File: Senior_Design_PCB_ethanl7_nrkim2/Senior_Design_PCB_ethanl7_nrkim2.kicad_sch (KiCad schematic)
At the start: 15 parts, among them U1 uA7805, U2 LM386, U3 L298N, U4 L298N, U5 L298N, U6 STM32H7B0RBTx, U7 LM2937xT

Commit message: changes to schematic
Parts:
- C1: value C -> .33 uF
- C2, C3: value C -> .1 uF
- C4: value C -> 10 uF
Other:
- moved on the sheet: C1
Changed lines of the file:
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@@
 	)
 	(junction
-		(at 53.34 50.8)
+		(at 49.53 50.8)
 		(diameter 0)
 		(color 0 0 0 0)
@@
 	(wire
 		(pts
-			(xy 53.34 62.23) (xy 64.77 62.23)
+			(xy 49.53 62.23) (xy 64.77 62.23)
 		)
 		(stroke
@@
 	(wire
 		(pts
-			(xy 53.34 50.8) (xy 57.15 50.8)
-		)
-		(stroke
-			(width 0)
-			(type default)
-		)
-	)
-	(wire
-		(pts
 			(xy 160.02 254) (xy 160.02 259.08)
 		)
@@
 	(wire
 		(pts
+			(xy 49.53 50.8) (xy 57.15 50.8)
+		)
+		(stroke
+			(width 0)
+			(type default)
+		)
+	)
+	(wire
+		(pts
 			(xy 80.01 213.36) (xy 80.01 218.44)
 		)
@@
 	(wire
 		(pts
-			(xy 53.34 52.07) (xy 53.34 50.8)
-		)
-		(stroke
-			(width 0)
-			(type default)
-		)
-	)
-	(wire
-		(pts
-			(xy 45.72 50.8) (xy 53.34 50.8)
+			(xy 49.53 52.07) (xy 49.53 50.8)
+		)
+		(stroke
+			(width 0)
+			(type default)
+		)
+	)
+	(wire
+		(pts
+			(xy 45.72 50.8) (xy 49.53 50.8)
 		)
 		(stroke
@@
 	(wire
 		(pts
-			(xy 53.34 62.23) (xy 53.34 59.69)
+			(xy 49.53 62.23) (xy 49.53 59.69)
 		)
 		(stroke
@@
 			)
 		)
-		(property "Value" "C"
+		(property "Value" ".1 uF"
 			(at 81.28 57.1499 0)
 			(effects
@@
 			)
 		)
-		(property "Value" "C"
+		(property "Value" ".1 uF"
 			(at 114.3 58.4199 0)
 			(effects
@@
 	(symbol
 		(lib_id "Device:C")
-		(at 53.34 55.88 0)
+		(at 49.53 55.88 0)
 		(unit 1)
 		(exclude_from_sim no)
@@
 		(fields_autoplaced yes)
 		(property "Reference" "C1"
-			(at 57.15 54.6099 0)
+			(at 53.34 54.6099 0)
 			(effects
 				(font
@@
 			)
 		)
-		(property "Value" "C"
-			(at 57.15 57.1499 0)
+		(property "Value" ".33 uF"
+			(at 53.34 57.1499 0)
 			(effects
 				(font
@@
 		)
 		(property "Footprint" ""
-			(at 54.3052 59.69 0)
+			(at 50.4952 59.69 0)
 			(effects
 				(font
@@
 		)
 		(property "Datasheet" "~"
-			(at 53.34 55.88 0)
+			(at 49.53 55.88 0)
 			(effects
 				(font
@@
 		)
 		(property "Description" "Unpolarized capacitor"
-			(at 53.34 55.88 0)
+			(at 49.53 55.88 0)
 			(effects
 				(font
@@
 			)
 		)
-		(property "Value" "C"
+		(property "Value" "10 uF"
 			(at 138.43 58.4199 0)
 			(effects

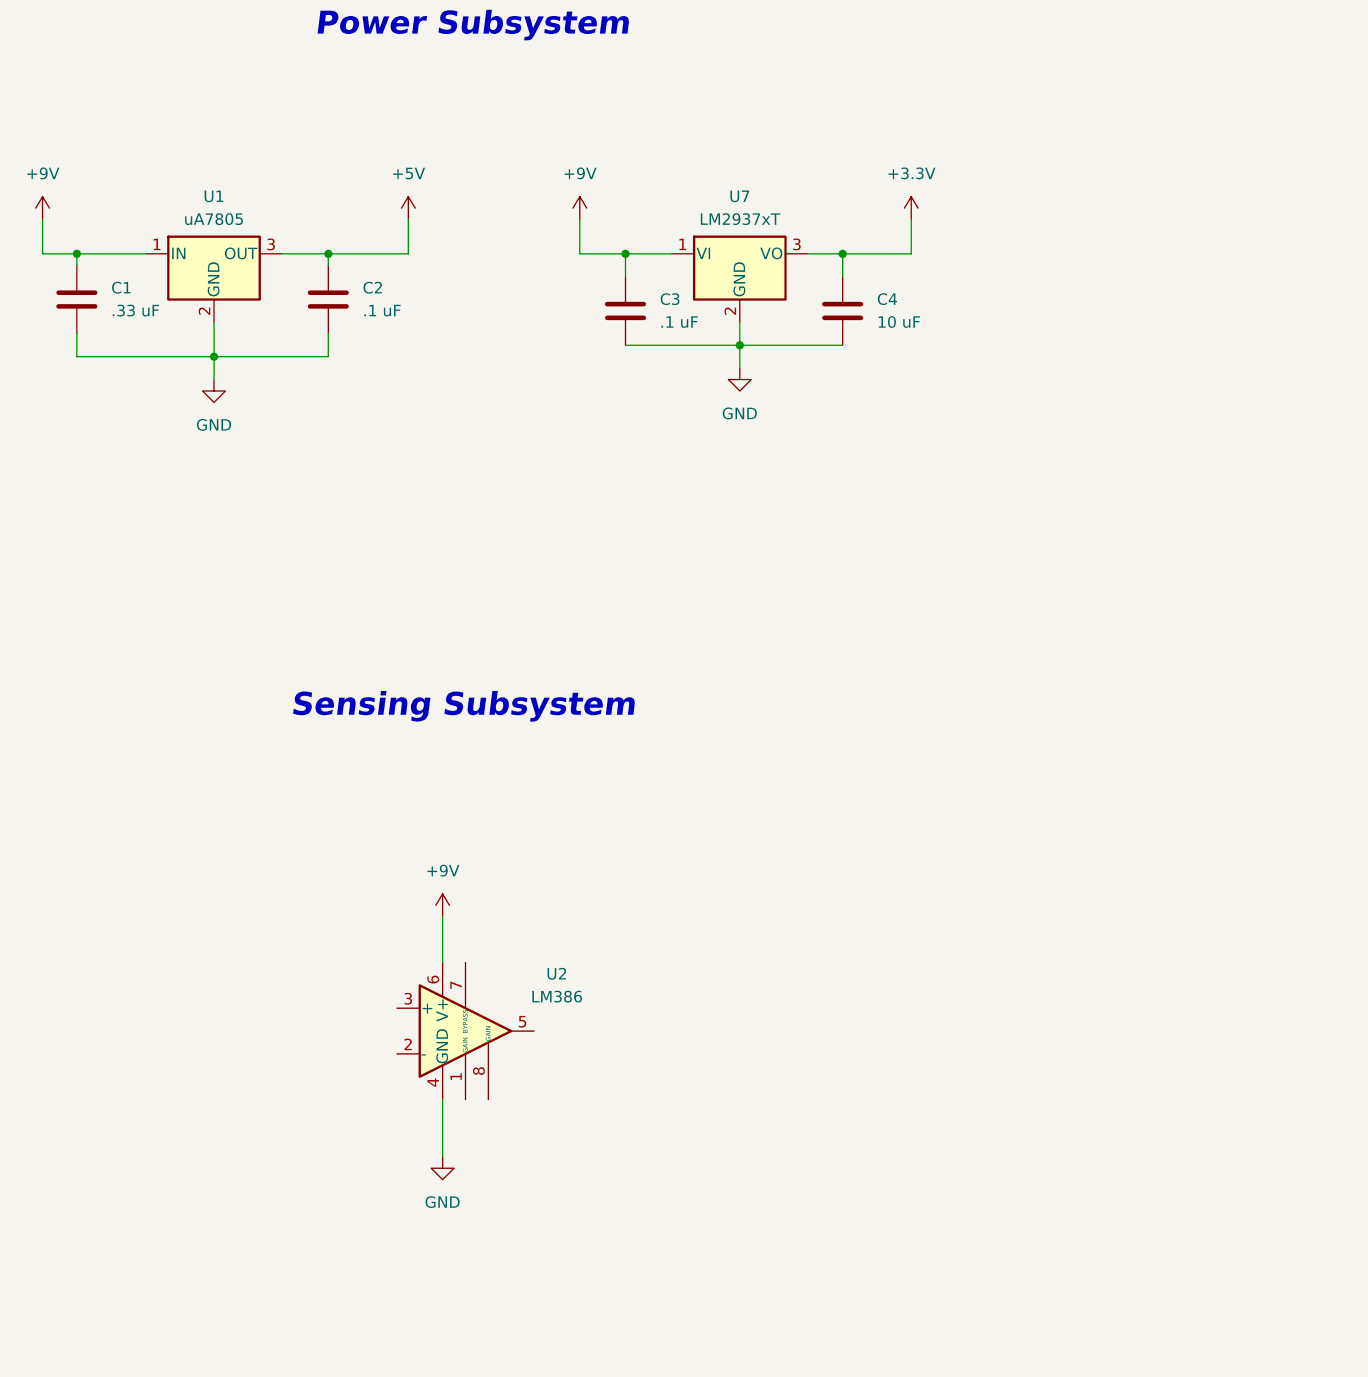
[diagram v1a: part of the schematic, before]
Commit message: schematic power supply and sensing
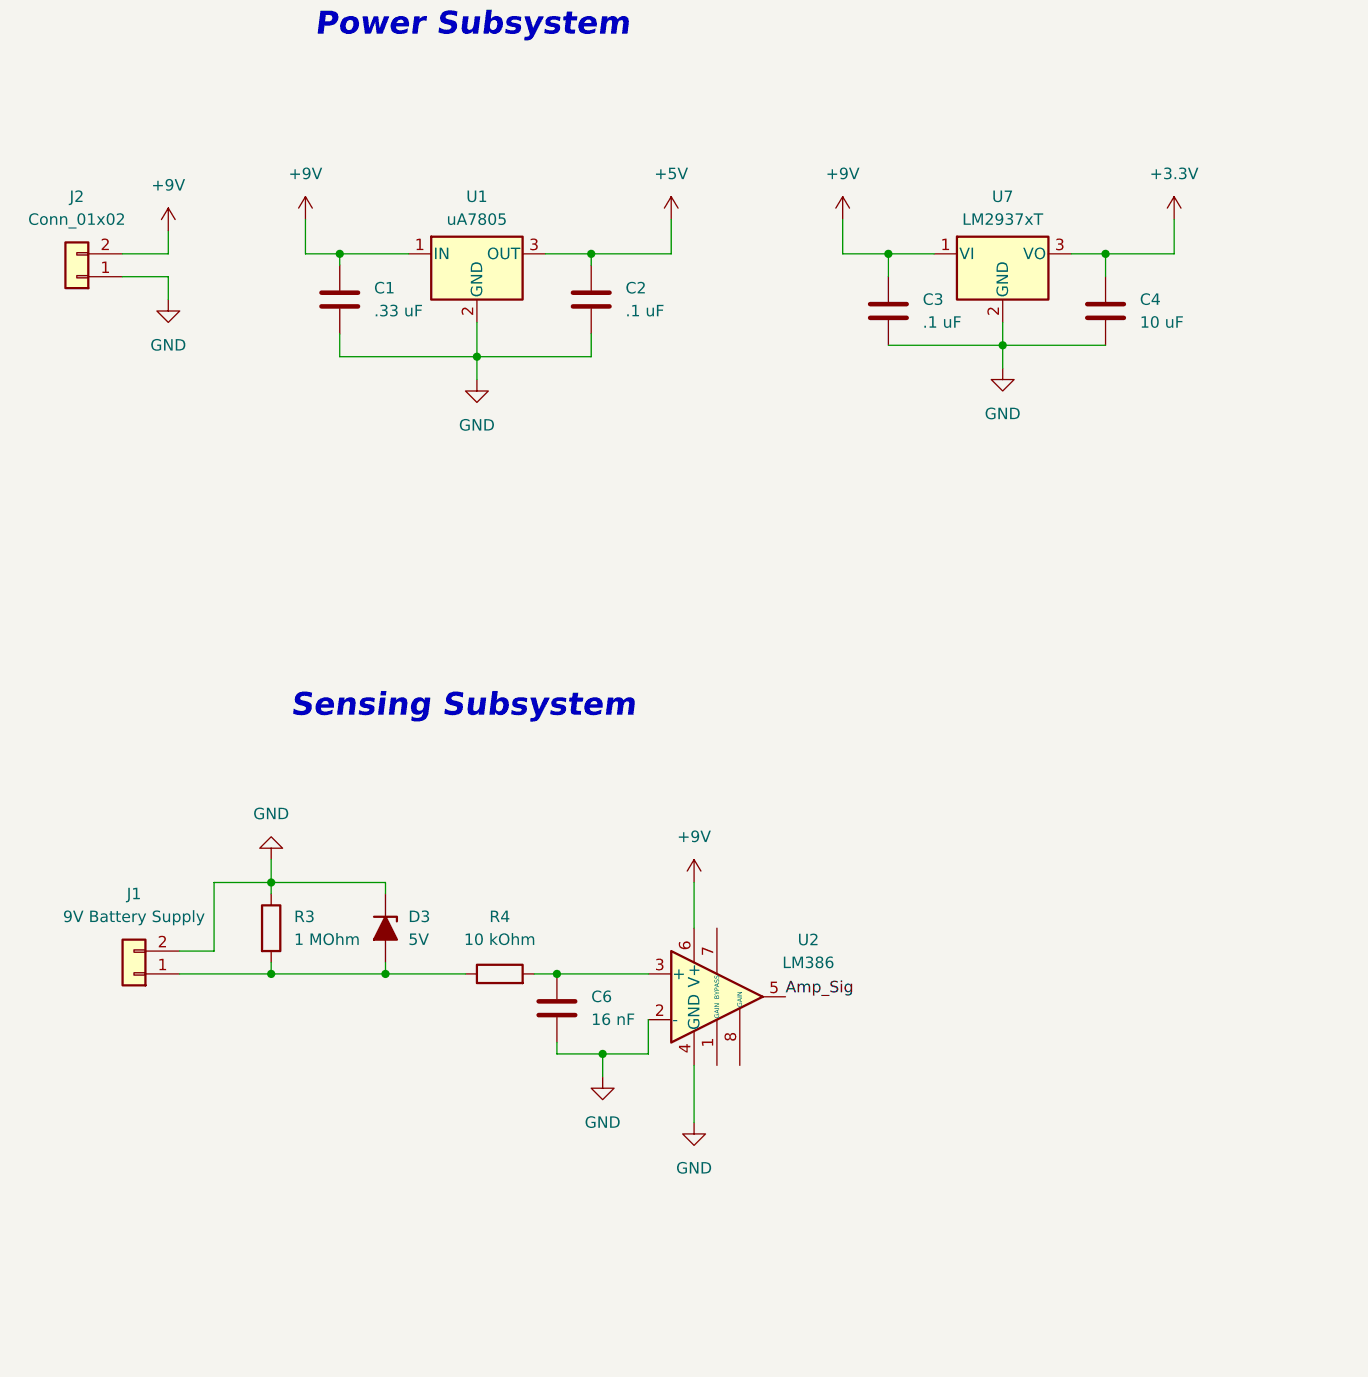
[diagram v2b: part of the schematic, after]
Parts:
- added C6: 16 nF, symbol Device:C
- added D3: 5V, symbol Device:D_Zener_Filled
- added J1: 9V Battery Supply, symbol Connector_Generic:Conn_01x02
- added J2: Conn_01x02, symbol Connector_Generic:Conn_01x02
- added R3: 1 MOhm, symbol Device:R
- added R4: 10 kOhm, symbol Device:R
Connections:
- net +9V: now also J2.2 (Pin_2)
- net GND: now also U2.2 (-), C6.1, D3.1 (K), J1.2 (Pin_2), J2.1 (Pin_1), R3.1
- net at U2.3 (+): now also C6.2, R4.2
- net Amp_Sig: now reaches U2.5
- new net: D3.2 (A), J1.1 (Pin_1), R3.2, R4.1
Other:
- moved on the sheet: C1, C2, C3, C4, U1, U2, U7

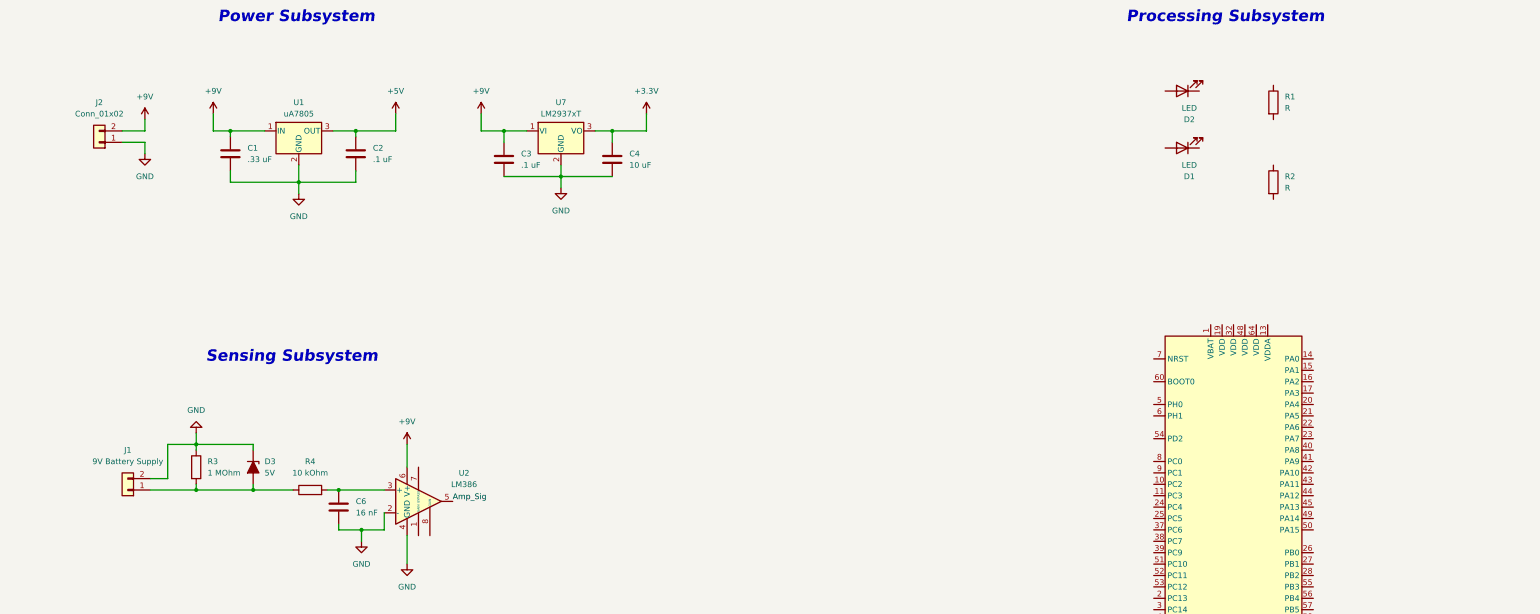
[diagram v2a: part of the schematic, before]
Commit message: scopy spectrogram data, slight updates to magnet mount and PCB schematic
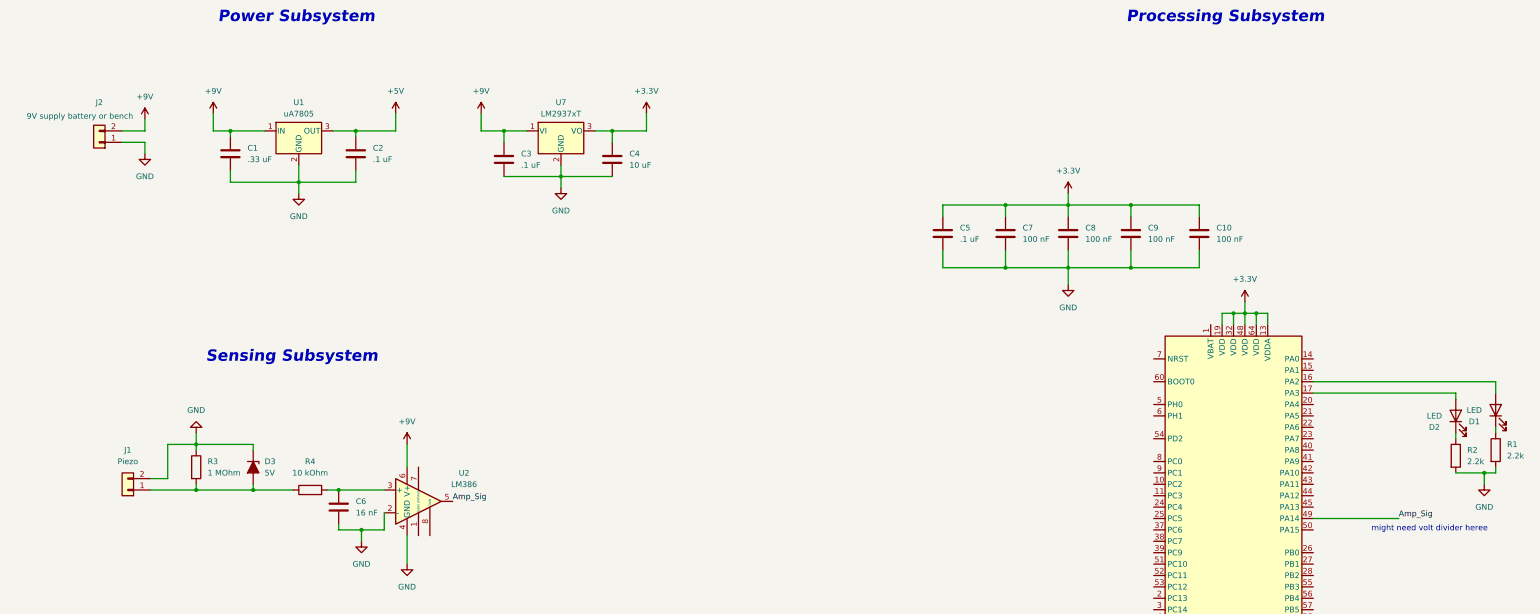
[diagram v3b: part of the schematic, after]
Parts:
- added C10, C7, C8, C9: 100 nF, symbol Device:C
- added C5: .1 uF, symbol Device:C
- J1: value 9V Battery Supply -> Piezo
- J2: value Conn_01x02 -> 9V supply battery or bench
- R1, R2: value R -> 2.2k
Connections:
- net +3.3V: now also U6.13 (VDDA), U6.19 (VDD), U6.32 (VDD), U6.48 (VDD), U6.64 (VDD), C10.1, C5.1, C7.1, C8.1, C9.1
- net Amp_Sig: now also U6.49 (PA14)
- net GND: now also R1.2, R2.2, C10.2, C5.2, C7.2, C8.2, C9.2
- net at D1.1 (K): now also R1.1
- net at D1.2 (A): now also U6.16 (PA2)
- net at U6.17 (PA3): now also D2.2 (A)
- net at D2.1 (K): now also R2.1
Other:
- note added: "might need volt divider heree"
- moved on the sheet: D1, D2, R1, R2

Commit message: schematic updates
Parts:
- added C11, C12: 1 uF, symbol Device:C
- added D4: MBR0520, Diode_SMD:D_SOD-123, symbol Diode:MBR0520
- added J3: Conn_02x03_Odd_Even, symbol Connector_Generic:Conn_02x03_Odd_Even
- added J4: Conn_ARM_JTAG_SWD_10, symbol Connector:Conn_ARM_JTAG_SWD_10
- added R10, R8, R9: 100 kOhm, symbol Device:R
- added R5, R6, R7: 10 kOhm, symbol Device:R
- added SW1: SW_Push, symbol Switch:SW_Push
- added TP1: GND, symbol Connector:TestPoint
- C10: value 100 nF -> 10 nF
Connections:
- net +3.3V: now also U6.60 (BOOT0), C11.1, J3.1 (Pin_1), J3.2 (Pin_2), R5.1
- net Amp_Sig: now also U6.8 (PC0); no longer U6.49 (PA14)
- net GND: now also U6.12 (VSSA), U6.18 (VSS), U6.31 (VSS), U6.47 (VSS), U6.63 (VSS), C11.2, C12.2, J3.5 (Pin_5), J3.6 (Pin_6), J4.3 (GND), J4.5 (GND), J4.9 (GNDDetect), R6.1, R7.2, SW1.1, TP1.1
- net JTMS/SWDIO: now reaches U6.45 (PA13)
- net JTMS/SWDIO: now also J4.2 (SWDIO/TMS), R9.1
- net JTDI: now reaches U6.50 (PA15)
- net JTDI: now also J4.8 (NC/TDI)
- net JTDO/TRACESWO: now reaches U6.55 (PB3)
- net JTDO/TRACESWO: now also J4.6 (SWO/TDO), R10.1
- net NRST: now reaches U6.7 (NRST)
- net NRST: now also C12.1, J4.10 (~{RESET}), R5.2, SW1.2
- new net: J3.3 (Pin_3), R6.2
- new net: D4.1 (K), R10.2, R8.2, R9.2
- new net: J3.4 (Pin_4), R7.1
- new net: D4.2 (A), J4.1 (VTref)
- new net JTCK/SWCLK: J4.4 (SWCLK/TCK), R8.1, U6.49 (PA14)
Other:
- note added: "might need volt divider"
- note removed: "might need volt divider heree"
- moved on the sheet: C5, C7, C8, C9, D1, D2, R1, R2, U3, U4, U5, U6

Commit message: finished schematic, started pcb
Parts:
- added C13, C14, C15, C16, C17, C18: 100 nF, Capacitor_SMD:C_0805_2012Metric_Pad1.18x1.45mm_HandSolder, symbol Device:C
- added D10, D11, D12, D13, D14, D15, D16, D17, D18, D19, D20, D21, D22, D23, D24, D25, D26, D27, D28, D5, D6, D7, D8, D9: 1N5817, Diode_THT:D_DO-41_SOD81_P10.16mm_Horizontal, symbol Diode:1N5817
- added H1, H2, H3, H4: MountingHole, MountingHole:MountingHole_3.2mm_M3, symbol Mechanical:MountingHole
- added J10: M6, Connector_Molex:Molex_KK-254_AE-6410-02A_1x02_P2.54mm_Vertical, symbol Connector_Generic:Conn_01x02
- added J5: M1, Connector_Molex:Molex_KK-254_AE-6410-02A_1x02_P2.54mm_Vertical, symbol Connector_Generic:Conn_01x02
- added J6: M2, Connector_Molex:Molex_KK-254_AE-6410-02A_1x02_P2.54mm_Vertical, symbol Connector_Generic:Conn_01x02
- added J7: M3, Connector_Molex:Molex_KK-254_AE-6410-02A_1x02_P2.54mm_Vertical, symbol Connector_Generic:Conn_01x02
- added J8: M4, Connector_Molex:Molex_KK-254_AE-6410-02A_1x02_P2.54mm_Vertical, symbol Connector_Generic:Conn_01x02
- added J9: M5, Connector_Molex:Molex_KK-254_AE-6410-02A_1x02_P2.54mm_Vertical, symbol Connector_Generic:Conn_01x02
- added TP2: AMP, TestPoint:TestPoint_Pad_D1.5mm, symbol Connector:TestPoint
- added TP3: LPF, TestPoint:TestPoint_Pad_D1.5mm, symbol Connector:TestPoint
- added TP4: Reg_5, TestPoint:TestPoint_Pad_D1.5mm, symbol Connector:TestPoint
- added TP5: Reg_3, TestPoint:TestPoint_Pad_D1.5mm, symbol Connector:TestPoint
- C1, C10, C11, C12, C2, C3, C4, C5, C6, C7, C8, C9: footprint (none) -> Capacitor_SMD:C_0805_2012Metric_Pad1.18x1.45mm_HandSolder
- D1, D2: footprint (none) -> LED_SMD:LED_0805_2012Metric_Pad1.15x1.40mm_HandSolder
- D3: value 5V -> 5V_Znr; footprint (none) -> Diode_THT:D_DO-41_SOD81_P10.16mm_Horizontal
- J1, J2: footprint (none) -> Connector_Molex:Molex_KK-254_AE-6410-02A_1x02_P2.54mm_Vertical
- J3: footprint (none) -> Connector_PinSocket_2.54mm:PinSocket_2x03_P2.54mm_Vertical
- J4: footprint (none) -> Connector_IDC:IDC-Header_2x05_P2.54mm_Vertical
- R1, R10, R2, R3, R4, R5, R6, R7, R8, R9: footprint (none) -> Resistor_SMD:R_0805_2012Metric_Pad1.20x1.40mm_HandSolder
- SW1: footprint (none) -> Button_Switch_SMD:SW_SPST_B3S-1000
- TP1: footprint (none) -> TestPoint:TestPoint_Pad_D1.5mm
- U1: footprint (none) -> Package_TO_SOT_THT:TO-220-3_Vertical
- U2: footprint (none) -> Package_DIP:DIP-8_W7.62mm
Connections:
- net +3.3V: now also D4.1 (K), R10.2, R8.2, R9.2, TP5.1
- net +5V: now also U2.6 (V+), U3.9 (Vss), U4.9 (Vss), U5.9 (Vss), C13.2, C15.2, C17.2, D11.1 (K), D13.1 (K), D15.1 (K), D17.1 (K), D19.1 (K), D21.1 (K), D23.1 (K), D25.1 (K), D27.1 (K), D7.1 (K), D8.1 (K), D9.1 (K), TP4.1; no longer U3.4 (Vs), U4.4 (Vs), U5.4 (Vs)
- net +9V: now also U3.4 (Vs), U4.4 (Vs), U5.4 (Vs), C14.1, C16.1, C18.1; no longer U2.6 (V+)
- net Amp_Sig: now also TP2.1
- net GND: now also C13.1, C14.2, C15.1, C16.2, C17.1, C18.2, D10.2 (A), D12.2 (A), D14.2 (A), D16.2 (A), D18.2 (A), D20.2 (A), D22.2 (A), D24.2 (A), D26.2 (A), D28.2 (A), D5.2 (A), D6.2 (A)
- net at D1.2 (A): now also U6.57 (PB5); no longer U6.16 (PA2)
- net M4P: now reaches U4.10 (IN3)
- net M4P: now also U6.37 (PC6)
- net M4En: now reaches U4.11 (EnB)
- net M4En: now also U6.17 (PA3)
- net M4N: now reaches U4.12 (IN4)
- net M4N: now also U6.38 (PC7)
- net at U4.13 (OUT3): now also D17.2 (A), D18.1 (K), J8.1 (Pin_1)
- net at U4.14 (OUT4): now also D19.2 (A), D20.1 (K), J8.2 (Pin_2)
- net at U4.2 (OUT1): now also D13.2 (A), D14.1 (K), J7.1 (Pin_1)
- net at U4.3 (OUT2): now also D15.2 (A), D16.1 (K), J7.2 (Pin_2)
- net M3P: now reaches U4.5 (IN1)
- net M3P: now also U6.35 (PB14)
- net M3En: now reaches U4.6 (EnA)
- net M3En: now also U6.16 (PA2)
- net M3N: now reaches U4.7 (IN2)
- net M3N: now also U6.36 (PB15)
- net at C6.2, R4.2, U2.3 (+): now also TP3.1
- net M1En: now reaches U6.14 (PA0)
- net M1En: now also U3.6 (EnA)
- net M2En: now reaches U6.15 (PA1)
- net M2En: now also U3.11 (EnB)
- net at D2.2 (A): now also U6.58 (PB6); no longer U6.17 (PA3)
- net M5En: now reaches U6.23 (PA7)
- net M5En: now also U5.6 (EnA)
- net M6En: now reaches U6.26 (PB0)
- net M6En: now also U5.11 (EnB)
- net M1P: now reaches U6.27 (PB1)
- net M1P: now also U3.5 (IN1)
- net M1N: now reaches U6.28 (PB2)
- net M1N: now also U3.7 (IN2)
- net M2P: now reaches U6.29 (PB10)
- net M2P: now also U3.10 (IN3)
- net M2N: now reaches U6.33 (PB12)
- net M2N: now also U3.12 (IN4)
- net M5P: now reaches U6.41 (PA9)
- net M5P: now also U5.5 (IN1)
- net M5N: now reaches U6.42 (PA10)
- net M5N: now also U5.7 (IN2)
- net M6P: now reaches U6.51 (PC10)
- net M6P: now also U5.10 (IN3)
- net M6N: now reaches U6.52 (PC11)
- net M6N: now also U5.12 (IN4)
- net at U5.13 (OUT3): now also D25.2 (A), D26.1 (K), J10.1 (Pin_1)
- net at U5.14 (OUT4): now also D27.2 (A), D28.1 (K), J10.2 (Pin_2)
- net at U5.2 (OUT1): now also D21.2 (A), D22.1 (K), J9.1 (Pin_1)
- net at U5.3 (OUT2): now also D23.2 (A), D24.1 (K), J9.2 (Pin_2)
- net at U3.13 (OUT3): now also D10.1 (K), D9.2 (A), J6.1 (Pin_1)
- net at U3.14 (OUT4): now also D11.2 (A), D12.1 (K), J6.2 (Pin_2)
- net at U3.2 (OUT1): now also D5.1 (K), D7.2 (A), J5.1 (Pin_1)
- net at U3.3 (OUT2): now also D6.1 (K), D8.2 (A), J5.2 (Pin_2)
- no-connect marks 0 -> 30
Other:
- note added: "Dubug Subsystem"
- title: (none) -> Automatic Guitar Tuner
- moved on the sheet: C1, C12, C2, C3, C4, C6, D1, D2, D3, D4, J1, J2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
